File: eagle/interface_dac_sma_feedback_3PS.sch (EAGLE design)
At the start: 25 parts, among them IC1 ISO1540, T1 TIP122V, T3 TIP122V, X1 BU-SMA-V

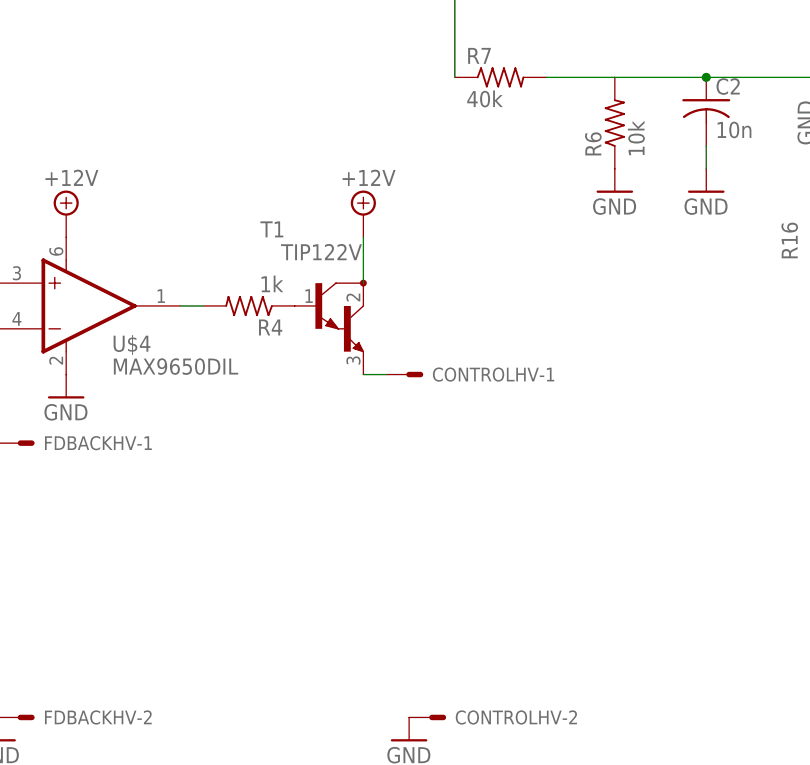
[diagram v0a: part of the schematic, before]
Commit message: 3PS, 2 1kV in parallel
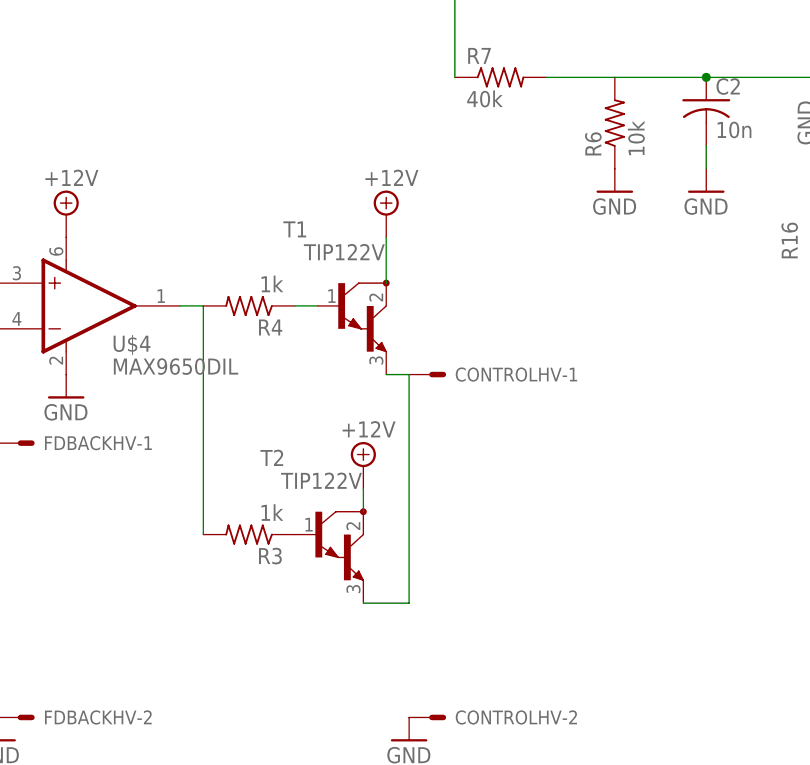
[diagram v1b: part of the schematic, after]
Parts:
- added R3: 1k, resistor:R-US_0207/12
- added T2: TIP122V, transistor-npn:TIP122V
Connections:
- new net N$6: R3.1, T2.B
- net +12V: now also T2.C
- net N$19: now also R3.2
- net N$4: now also T2.E
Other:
- moved on the sheet: CONTROLHV-1, T1
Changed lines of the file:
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@@
 <part name="GND11" library="supply1" deviceset="GND" device=""/>
 <part name="OK2" library="optocoupler" deviceset="H11F1" device=""/>
+<part name="T2" library="transistor-npn" deviceset="TIP122*" device="V" value="TIP122V"/>
+<part name="P+4" library="supply2" deviceset="+12V" device=""/>
+<part name="R3" library="resistor" deviceset="R-US_" device="0207/12" value="1k"/>
 </parts>
 <sheets>
@@
 <instance part="R1" gate="G$1" x="48.26" y="33.02" rot="R90"/>
 <instance part="R2" gate="G$1" x="55.88" y="30.48" rot="R90"/>
-<instance part="T1" gate="G$1" x="195.58" y="68.58"/>
-<instance part="P+3" gate="+12V" x="200.66" y="78.74"/>
+<instance part="T1" gate="G$1" x="198.12" y="68.58"/>
+<instance part="P+3" gate="+12V" x="203.2" y="78.74"/>
 <instance part="T3" gate="G$1" x="203.2" y="-27.94"/>
 <instance part="P+12" gate="+12V" x="208.28" y="-22.86"/>
 <instance part="R4" gate="G$1" x="187.96" y="68.58" rot="R180"/>
 <instance part="R14" gate="G$1" x="185.42" y="-27.94" rot="R180"/>
-<instance part="CONTROLHV" gate="-1" x="205.74" y="60.96"/>
+<instance part="CONTROLHV" gate="-1" x="208.28" y="60.96"/>
 <instance part="CONTROLHV" gate="-2" x="208.28" y="22.86"/>
 <instance part="CONTROLHV" gate="-3" x="218.44" y="-35.56"/>
@@
 <instance part="GND11" gate="1" x="238.76" y="81.28"/>
 <instance part="OK2" gate="G$1" x="27.94" y="-76.2"/>
+<instance part="T2" gate="G$1" x="195.58" y="43.18"/>
+<instance part="P+4" gate="+12V" x="200.66" y="50.8"/>
+<instance part="R3" gate="G$1" x="187.96" y="43.18" rot="R180"/>
 </instances>
 <busses>
@@
 <pinref part="T1" gate="G$1" pin="C"/>
 <pinref part="P+3" gate="+12V" pin="+12V"/>
-<wire x1="200.66" y1="76.2" x2="200.66" y2="71.12" width="0.1524" layer="91"/>
+<wire x1="203.2" y1="76.2" x2="203.2" y2="71.12" width="0.1524" layer="91"/>
 </segment>
 <segment>
 <pinref part="T3" gate="G$1" pin="C"/>
 <pinref part="P+12" gate="+12V" pin="+12V"/>
+</segment>
+<segment>
+<pinref part="T2" gate="G$1" pin="C"/>
+<pinref part="P+4" gate="+12V" pin="+12V"/>
+<wire x1="200.66" y1="48.26" x2="200.66" y2="45.72" width="0.1524" layer="91"/>
 </segment>
 </net>
@@
 <pinref part="R4" gate="G$1" pin="2"/>
 <wire x1="182.88" y1="68.58" x2="180.34" y2="68.58" width="0.1524" layer="91"/>
+<pinref part="R3" gate="G$1" pin="2"/>
+<wire x1="182.88" y1="68.58" x2="182.88" y2="43.18" width="0.1524" layer="91"/>
 </segment>
 </net>
@@
 <pinref part="T1" gate="G$1" pin="E"/>
 <pinref part="CONTROLHV" gate="-1" pin="S"/>
-<wire x1="200.66" y1="60.96" x2="203.2" y2="60.96" width="0.1524" layer="91"/>
+<wire x1="203.2" y1="60.96" x2="205.74" y2="60.96" width="0.1524" layer="91"/>
+</segment>
+<segment>
+<wire x1="205.74" y1="60.96" x2="205.74" y2="35.56" width="0.1524" layer="91"/>
+<pinref part="T2" gate="G$1" pin="E"/>
+<wire x1="205.74" y1="35.56" x2="200.66" y2="35.56" width="0.1524" layer="91"/>
 </segment>
 </net>
@@
 <pinref part="T1" gate="G$1" pin="B"/>
 <pinref part="R4" gate="G$1" pin="1"/>
-</segment>
-</net>
+<wire x1="195.58" y1="68.58" x2="193.04" y2="68.58" width="0.1524" layer="91"/>
+</segment>
+</net>
+<net name="N$6" class="0">
+<segment>
+<pinref part="T2" gate="G$1" pin="B"/>
+<pinref part="R3" gate="G$1" pin="1"/>
+</segment>
+</net>

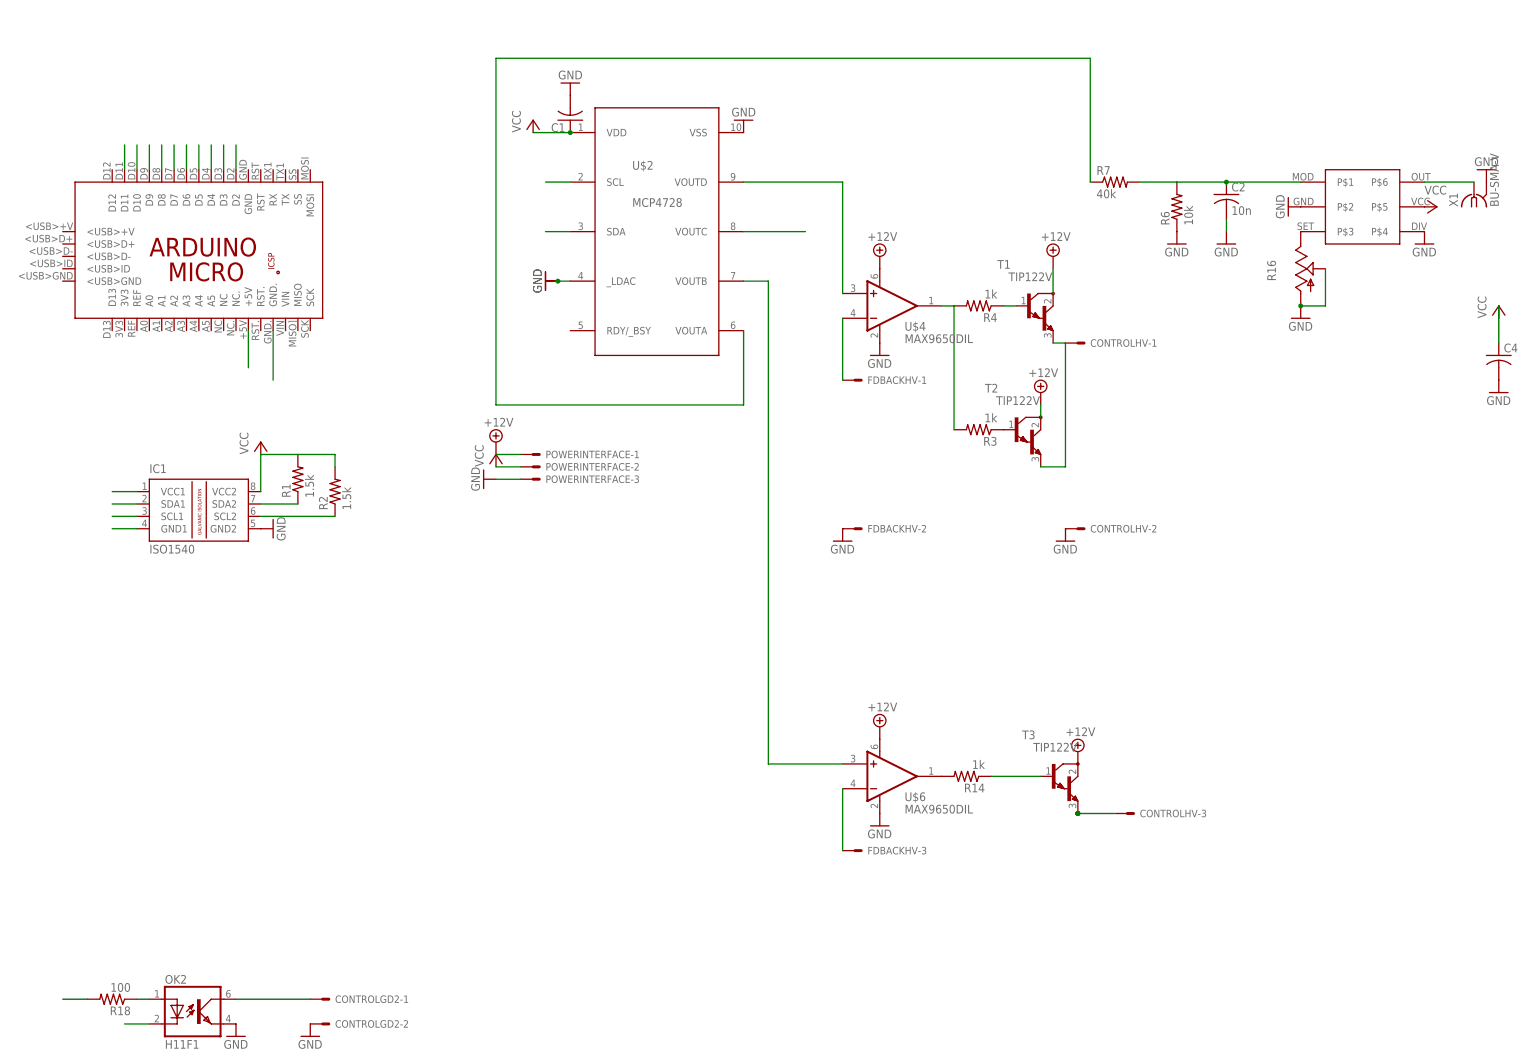
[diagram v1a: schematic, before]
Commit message: tweaks. still need bigger vias for zeners and hv resistors
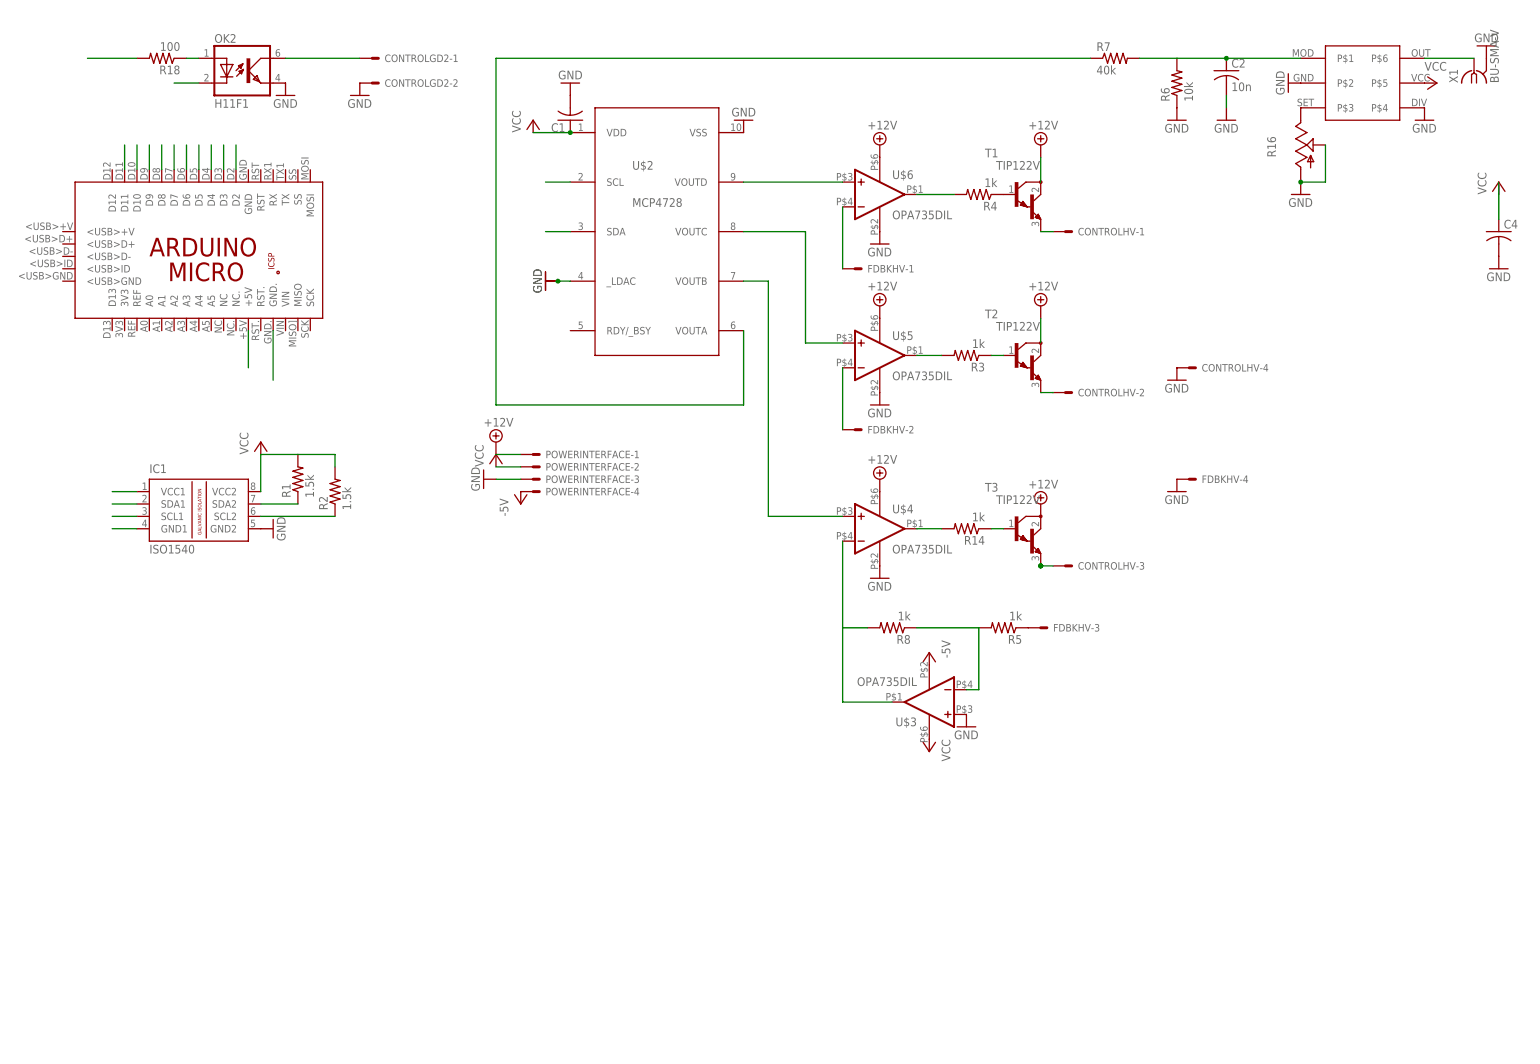
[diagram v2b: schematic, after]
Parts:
- removed FDBACKHV: (no value), con-molex:KK-156-3
- added FDBKHV: (no value), con-molex:KK-156-4
- added R5, R8: 1k, resistor:R-US_0207/12
- added U$3, U$5: OPA735DIL, texas:OPA735DIL
- CONTROLHV, POWERINTERFACE: device con-molex:KK-156-3 -> con-molex:KK-156-4
- U$4, U$6: value MAX9650DIL -> OPA735DIL; device maxim:MAX9650DIL -> texas:OPA735DIL
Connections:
- new net -5V: POWERINTERFACE-4.S, U$3.V-
- new net N$10: R3.2, U$5.OUT
- new net N$11: CONTROLHV-2.S, T2.E
- new net N$23: R5.2, R8.1, U$3.-IN
- new net N$6: FDBKHV-2.S, U$5.-IN
- new net N$9: FDBKHV-3.S, R5.1
- net +12V: now also U$5.V+
- net GND: now also CONTROLHV-4.S, FDBKHV-4.S, U$3.+IN, U$5.V-; no longer CONTROLHV-2.S, FDBACKHV-2.S
- net N$14: now also R8.2, U$3.OUT, U$4.-IN; no longer FDBACKHV-3.S, U$6.-IN
- net N$16: now also U$6.+IN; no longer U$4.+IN
- net N$17: now also U$5.+IN
- net N$18: now also U$4.+IN; no longer U$6.+IN
- net N$19: now also U$6.OUT; no longer R3.2, U$4.OUT
- net N$21: now also U$4.OUT; no longer U$6.OUT
- net N$4: no longer T2.E
- net N$8: now also FDBKHV-1.S, U$6.-IN; no longer FDBACKHV-1.S, U$4.-IN
- net VCC: now also U$3.V+
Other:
- moved on the sheet: C2, C4, CONTROLGD2-1, CONTROLGD2-2, CONTROLHV-1, CONTROLHV-2, CONTROLHV-3, OK2, R14, R16, R18, R3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

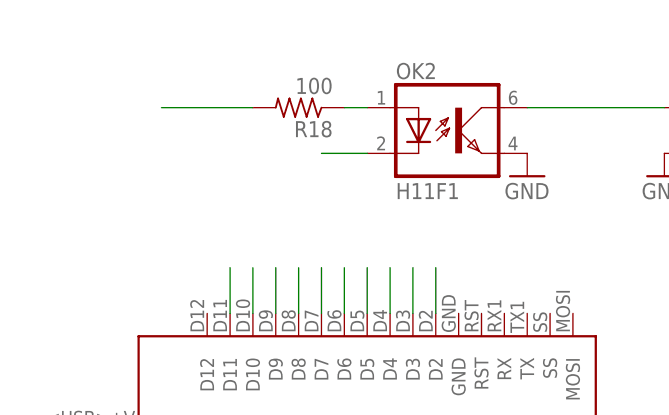
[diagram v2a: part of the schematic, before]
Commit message: layout fixes
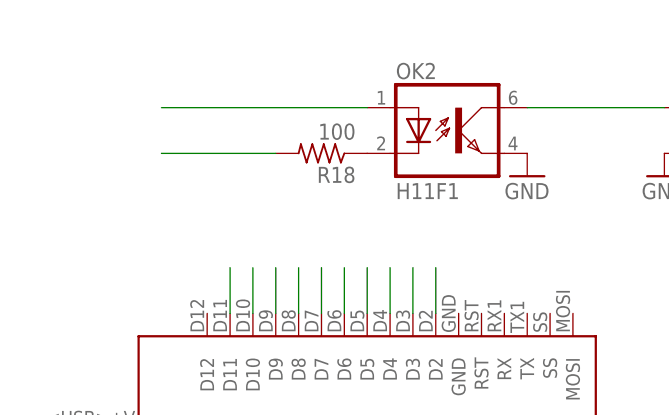
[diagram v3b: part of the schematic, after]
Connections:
- net N$7: now also OK2.C; no longer OK2.A
- net PWM9: now also OK2.A; no longer OK2.C
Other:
- moved on the sheet: R18
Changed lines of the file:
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@@
 <instance part="X1" gate="G$1" x="289.56" y="116.84" rot="R90"/>
 <instance part="GND17" gate="1" x="292.1" y="121.92" rot="R180"/>
-<instance part="R18" gate="G$1" x="20.32" y="119.38" rot="R180"/>
+<instance part="R18" gate="G$1" x="22.86" y="114.3" rot="R180"/>
 <instance part="GND1" gate="1" x="45.72" y="111.76"/>
 <instance part="CONTROLGD2" gate="-1" x="63.5" y="119.38"/>
@@
 <net name="AGND" class="0">
 <segment>
-<wire x1="5.08" y1="119.38" x2="15.24" y2="119.38" width="0.1524" layer="91"/>
+<wire x1="5.08" y1="114.3" x2="17.78" y2="114.3" width="0.1524" layer="91"/>
 <pinref part="R18" gate="G$1" pin="2"/>
 </segment>
@@
 </segment>
 <segment>
-<wire x1="27.94" y1="114.3" x2="22.86" y2="114.3" width="0.1524" layer="91"/>
-<pinref part="OK2" gate="G$1" pin="C"/>
+<wire x1="27.94" y1="119.38" x2="5.08" y2="119.38" width="0.1524" layer="91"/>
+<pinref part="OK2" gate="G$1" pin="A"/>
 </segment>
 </net>
@@
 <pinref part="X1" gate="G$1" pin="1"/>
 <wire x1="289.56" y1="119.38" x2="279.4" y2="119.38" width="0.1524" layer="91"/>
-</segment>
-</net>
-<net name="N$7" class="0">
-<segment>
-<pinref part="R18" gate="G$1" pin="1"/>
-<wire x1="27.94" y1="119.38" x2="25.4" y2="119.38" width="0.1524" layer="91"/>
-<pinref part="OK2" gate="G$1" pin="A"/>
 </segment>
 </net>
@@
 </segment>
 </net>
+<net name="N$7" class="0">
+<segment>
+<pinref part="OK2" gate="G$1" pin="C"/>
+<pinref part="R18" gate="G$1" pin="1"/>
+</segment>
+</net>
